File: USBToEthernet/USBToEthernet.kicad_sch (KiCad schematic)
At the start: 54 parts, among them J1 0480372200, J2 L836-1J1T-43, SW1 SW_Push, U1 LAN7500-ABJZ, U2 NCP1117-3.3_SOT223, U3 93LCxxAxxOT, U4 USBLC6-2SC6, U6 AMS1117-1.2, Y1 25Mhz

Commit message: Will redo layout
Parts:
- J1: footprint (none) -> USB_A_Plug:MOLEX_0480372200
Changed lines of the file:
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@@
 			)
 		)
-		(property "Footprint" ""
+		(property "Footprint" "USB_A_Plug:MOLEX_0480372200"
 			(at 19.812 16.256 0)
 			(effects

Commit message: Revamped the PCB
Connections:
- net TR0+: now also U1.43 (TR0P); no longer U1.44 (TR0P)
- net TR0-: now also U1.44 (TR0N); no longer U1.43 (TR0N)
- net TR2+: now also U1.51 (TR2P); no longer U1.52 (TR2P)
- net TR2-: now also U1.52 (TR2N); no longer U1.51 (TR2N)
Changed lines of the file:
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@@
 		)
 	)
-	(label "TR0-"
+	(label "TR0+"
 		(at 135.89 85.09 180)
 		(effects
@@
 		)
 	)
-	(label "TR2-"
+	(label "TR2+"
 		(at 135.89 100.33 180)
 		(effects
@@
 		)
 	)
-	(label "TR2+"
+	(label "TR2-"
 		(at 135.89 102.87 180)
 		(effects
@@
 		)
 	)
-	(label "TR0+"
+	(label "TR0-"
 		(at 135.89 87.63 180)
 		(effects
@@
 	)
 	(symbol
+		(lib_name "LAN7500-ABJZ_1")
 		(lib_id "Interface_Ethernet:LAN7500-ABJZ")
 		(at 53.34 101.6 0)
@@
 		(fields_autoplaced yes)
 		(property "Reference" "U1"
-			(at 55.4833 132.08 0)
+			(at 53.34 81.28 0)
 			(effects
 				(font
 					(size 1.27 1.27)
 				)
-				(justify left)
 			)
 		)
 		(property "Value" "LAN7500-ABJZ"
-			(at 55.4833 134.62 0)
+			(at 53.34 83.82 0)
 			(effects
 				(font
 					(size 1.27 1.27)
 				)
-				(justify left)
 			)
 		)

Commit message: Reroute again
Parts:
- C1, C10, C11, C12, C13, C14, C15, C16, C17, C18, C19, C2, C20, C21, C22, C23, C24, C25, C26, C27, C3, C4, C5, C6, C7, C8, C9: footprint Capacitor_SMD:C_0603_1608Metric -> Capacitor_SMD:C_0402_1005Metric
- FB1, FB2, FB3, FB4, FB5: footprint Inductor_SMD:L_0603_1608Metric -> Inductor_SMD:L_0402_1005Metric
- R1, R10, R11, R12, R13, R2, R3, R4, R5, R6, R7, R8, R9: footprint Resistor_SMD:R_0603_1608Metric -> Resistor_SMD:R_0402_1005Metric
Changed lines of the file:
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@@
 			)
 		)
-		(property "Footprint" "Capacitor_SMD:C_0603_1608Metric"
+		(property "Footprint" "Capacitor_SMD:C_0402_1005Metric"
 			(at 24.13 154.94 0)
 			(effects
@@
 			)
 		)
-		(property "Footprint" "Capacitor_SMD:C_0603_1608Metric"
+		(property "Footprint" "Capacitor_SMD:C_0402_1005Metric"
 			(at 129.54 160.02 0)
 			(effects
@@
 			)
 		)
-		(property "Footprint" "Inductor_SMD:L_0603_1608Metric"
+		(property "Footprint" "Inductor_SMD:L_0402_1005Metric"
 			(at 216.662 20.32 90)
 			(effects
@@
 			)
 		)
-		(property "Footprint" "Resistor_SMD:R_0603_1608Metric"
+		(property "Footprint" "Resistor_SMD:R_0402_1005Metric"
 			(at 99.06 109.22 0)
 			(effects
@@
 			)
 		)
-		(property "Footprint" "Capacitor_SMD:C_0603_1608Metric"
+		(property "Footprint" "Capacitor_SMD:C_0402_1005Metric"
 			(at 177.8 31.75 0)
 			(effects
@@
 			)
 		)
-		(property "Footprint" "Capacitor_SMD:C_0603_1608Metric"
+		(property "Footprint" "Capacitor_SMD:C_0402_1005Metric"
 			(at 30.48 154.94 0)
 			(effects
@@
 			)
 		)
-		(property "Footprint" "Capacitor_SMD:C_0603_1608Metric"
+		(property "Footprint" "Capacitor_SMD:C_0402_1005Metric"
 			(at 190.5 76.2 0)
 			(effects
@@
 			)
 		)
-		(property "Footprint" "Capacitor_SMD:C_0603_1608Metric"
+		(property "Footprint" "Capacitor_SMD:C_0402_1005Metric"
 			(at 63.5 154.94 0)
 			(effects
@@
 			)
 		)
-		(property "Footprint" "Resistor_SMD:R_0603_1608Metric"
+		(property "Footprint" "Resistor_SMD:R_0402_1005Metric"
 			(at 196.85 30.48 0)
 			(effects
@@
 			)
 		)
-		(property "Footprint" "Capacitor_SMD:C_0603_1608Metric"
+		(property "Footprint" "Capacitor_SMD:C_0402_1005Metric"
 			(at 90.17 35.56 0)
 			(effects
@@
 			)
 		)
-		(property "Footprint" "Capacitor_SMD:C_0603_1608Metric"
+		(property "Footprint" "Capacitor_SMD:C_0402_1005Metric"
 			(at 182.88 76.2 0)
 			(effects
@@
 			)
 		)
-		(property "Footprint" "Capacitor_SMD:C_0603_1608Metric"
+		(property "Footprint" "Capacitor_SMD:C_0402_1005Metric"
 			(at 17.78 154.94 0)
 			(effects
@@
 			)
 		)
-		(property "Footprint" "Capacitor_SMD:C_0603_1608Metric"
+		(property "Footprint" "Capacitor_SMD:C_0402_1005Metric"
 			(at 173.99 76.2 0)
 			(effects
@@
 			)
 		)
-		(property "Footprint" "Capacitor_SMD:C_0603_1608Metric"
+		(property "Footprint" "Capacitor_SMD:C_0402_1005Metric"
 			(at 121.92 185.42 0)
 			(effects
@@
 			)
 		)
-		(property "Footprint" "Capacitor_SMD:C_0603_1608Metric"
+		(property "Footprint" "Capacitor_SMD:C_0402_1005Metric"
 			(at 128.27 31.75 0)
 			(effects
@@
 			)
 		)
-		(property "Footprint" "Capacitor_SMD:C_0603_1608Metric"
+		(property "Footprint" "Capacitor_SMD:C_0402_1005Metric"
 			(at 69.85 184.15 0)
 			(effects
@@
 			)
 		)
-		(property "Footprint" "Capacitor_SMD:C_0603_1608Metric"
+		(property "Footprint" "Capacitor_SMD:C_0402_1005Metric"
 			(at 87.63 160.02 0)
 			(effects
@@
 			)
 		)
-		(property "Footprint" "Inductor_SMD:L_0603_1608Metric"
+		(property "Footprint" "Inductor_SMD:L_0402_1005Metric"
 			(at 82.042 149.86 90)
 			(effects
@@
 			)
 		)
-		(property "Footprint" "Capacitor_SMD:C_0603_1608Metric"
+		(property "Footprint" "Capacitor_SMD:C_0402_1005Metric"
 			(at 153.67 76.2 0)
 			(effects
@@
 			)
 		)
-		(property "Footprint" "Capacitor_SMD:C_0603_1608Metric"
+		(property "Footprint" "Capacitor_SMD:C_0402_1005Metric"
 			(at 210.82 31.75 0)
 			(effects
@@
 			)
 		)
-		(property "Footprint" "Capacitor_SMD:C_0603_1608Metric"
+		(property "Footprint" "Capacitor_SMD:C_0402_1005Metric"
 			(at 107.95 160.02 0)
 			(effects
@@
 			)
 		)
-		(property "Footprint" "Resistor_SMD:R_0603_1608Metric"
+		(property "Footprint" "Resistor_SMD:R_0402_1005Metric"
 			(at 264.16 30.48 0)
 			(effects
@@
 			)
 		)
-		(property "Footprint" "Capacitor_SMD:C_0603_1608Metric"
+		(property "Footprint" "Capacitor_SMD:C_0402_1005Metric"
 			(at 242.57 31.75 0)
 			(effects
@@
 			)
 		)
-		(property "Footprint" "Resistor_SMD:R_0603_1608Metric"
+		(property "Footprint" "Resistor_SMD:R_0402_1005Metric"
 			(at 200.66 30.48 0)
 			(effects
@@
 			)
 		)
-		(property "Footprint" "Capacitor_SMD:C_0603_1608Metric"
+		(property "Footprint" "Capacitor_SMD:C_0402_1005Metric"
 			(at 66.04 24.13 0)
 			(effects
@@
 			)
 		)
-		(property "Footprint" "Resistor_SMD:R_0603_1608Metric"
+		(property "Footprint" "Resistor_SMD:R_0402_1005Metric"
 			(at 260.35 30.48 0)
 			(effects
@@
 			)
 		)
-		(property "Footprint" "Capacitor_SMD:C_0603_1608Metric"
+		(property "Footprint" "Capacitor_SMD:C_0402_1005Metric"
 			(at 274.32 31.75 0)
 			(effects
@@
 			)
 		)
-		(property "Footprint" "Capacitor_SMD:C_0603_1608Metric"
+		(property "Footprint" "Capacitor_SMD:C_0402_1005Metric"
 			(at 107.95 34.29 0)
 			(effects
@@
 			)
 		)
-		(property "Footprint" "Resistor_SMD:R_0603_1608Metric"
+		(property "Footprint" "Resistor_SMD:R_0402_1005Metric"
 			(at 163.83 30.48 0)
 			(effects
@@
 			)
 		)
-		(property "Footprint" "Capacitor_SMD:C_0603_1608Metric"
+		(property "Footprint" "Capacitor_SMD:C_0402_1005Metric"
 			(at 36.83 154.94 0)
 			(effects
@@
 			)
 		)
-		(property "Footprint" "Capacitor_SMD:C_0603_1608Metric"
+		(property "Footprint" "Capacitor_SMD:C_0402_1005Metric"
 			(at 146.05 31.75 0)
 			(effects
@@
 			)
 		)
-		(property "Footprint" "Resistor_SMD:R_0603_1608Metric"
+		(property "Footprint" "Resistor_SMD:R_0402_1005Metric"
 			(at 241.3 93.98 0)
 			(effects
@@
 			)
 		)
-		(property "Footprint" "Resistor_SMD:R_0603_1608Metric"
+		(property "Footprint" "Resistor_SMD:R_0402_1005Metric"
 			(at 242.57 86.36 0)
 			(effects
@@
 			)
 		)
-		(property "Footprint" "Capacitor_SMD:C_0603_1608Metric"
+		(property "Footprint" "Capacitor_SMD:C_0402_1005Metric"
 			(at 43.18 154.94 0)
 			(effects
@@
 			)
 		)
-		(property "Footprint" "Capacitor_SMD:C_0603_1608Metric"
+		(property "Footprint" "Capacitor_SMD:C_0402_1005Metric"
 			(at 87.63 184.15 0)
 			(effects
@@
 			)
 		)
-		(property "Footprint" "Resistor_SMD:R_0603_1608Metric"
+		(property "Footprint" "Resistor_SMD:R_0402_1005Metric"
 			(at 91.44 106.68 0)
 			(effects
@@
 			)
 		)
-		(property "Footprint" "Capacitor_SMD:C_0603_1608Metric"
+		(property "Footprint" "Capacitor_SMD:C_0402_1005Metric"
 			(at 49.53 154.94 0)
 			(effects
@@
 			)
 		)
-		(property "Footprint" "Inductor_SMD:L_0603_1608Metric"
+		(property "Footprint" "Inductor_SMD:L_0402_1005Metric"
 			(at 102.362 149.86 90)
 			(effects
@@
 			)
 		)
-		(property "Footprint" "Capacitor_SMD:C_0603_1608Metric"
+		(property "Footprint" "Capacitor_SMD:C_0402_1005Metric"
 			(at 198.12 76.2 0)
 			(effects
@@
 			)
 		)
-		(property "Footprint" "Inductor_SMD:L_0603_1608Metric"
+		(property "Footprint" "Inductor_SMD:L_0402_1005Metric"
 			(at 148.082 67.31 90)
 			(effects
@@
 			)
 		)
-		(property "Footprint" "Resistor_SMD:R_0603_1608Metric"
+		(property "Footprint" "Resistor_SMD:R_0402_1005Metric"
 			(at 228.6 30.48 0)
 			(effects
@@
 			)
 		)
-		(property "Footprint" "Resistor_SMD:R_0603_1608Metric"
+		(property "Footprint" "Resistor_SMD:R_0402_1005Metric"
 			(at 167.64 30.48 0)
 			(effects
@@
 			)
 		)
-		(property "Footprint" "Resistor_SMD:R_0603_1608Metric"
+		(property "Footprint" "Resistor_SMD:R_0402_1005Metric"
 			(at 121.92 175.26 0)
 			(effects
@@
 			)
 		)
-		(property "Footprint" "Resistor_SMD:R_0603_1608Metric"
+		(property "Footprint" "Resistor_SMD:R_0402_1005Metric"
 			(at 232.41 30.48 0)
 			(effects
@@
 			)
 		)
-		(property "Footprint" "Inductor_SMD:L_0603_1608Metric"
+		(property "Footprint" "Inductor_SMD:L_0402_1005Metric"
 			(at 123.952 151.13 90)
 			(effects

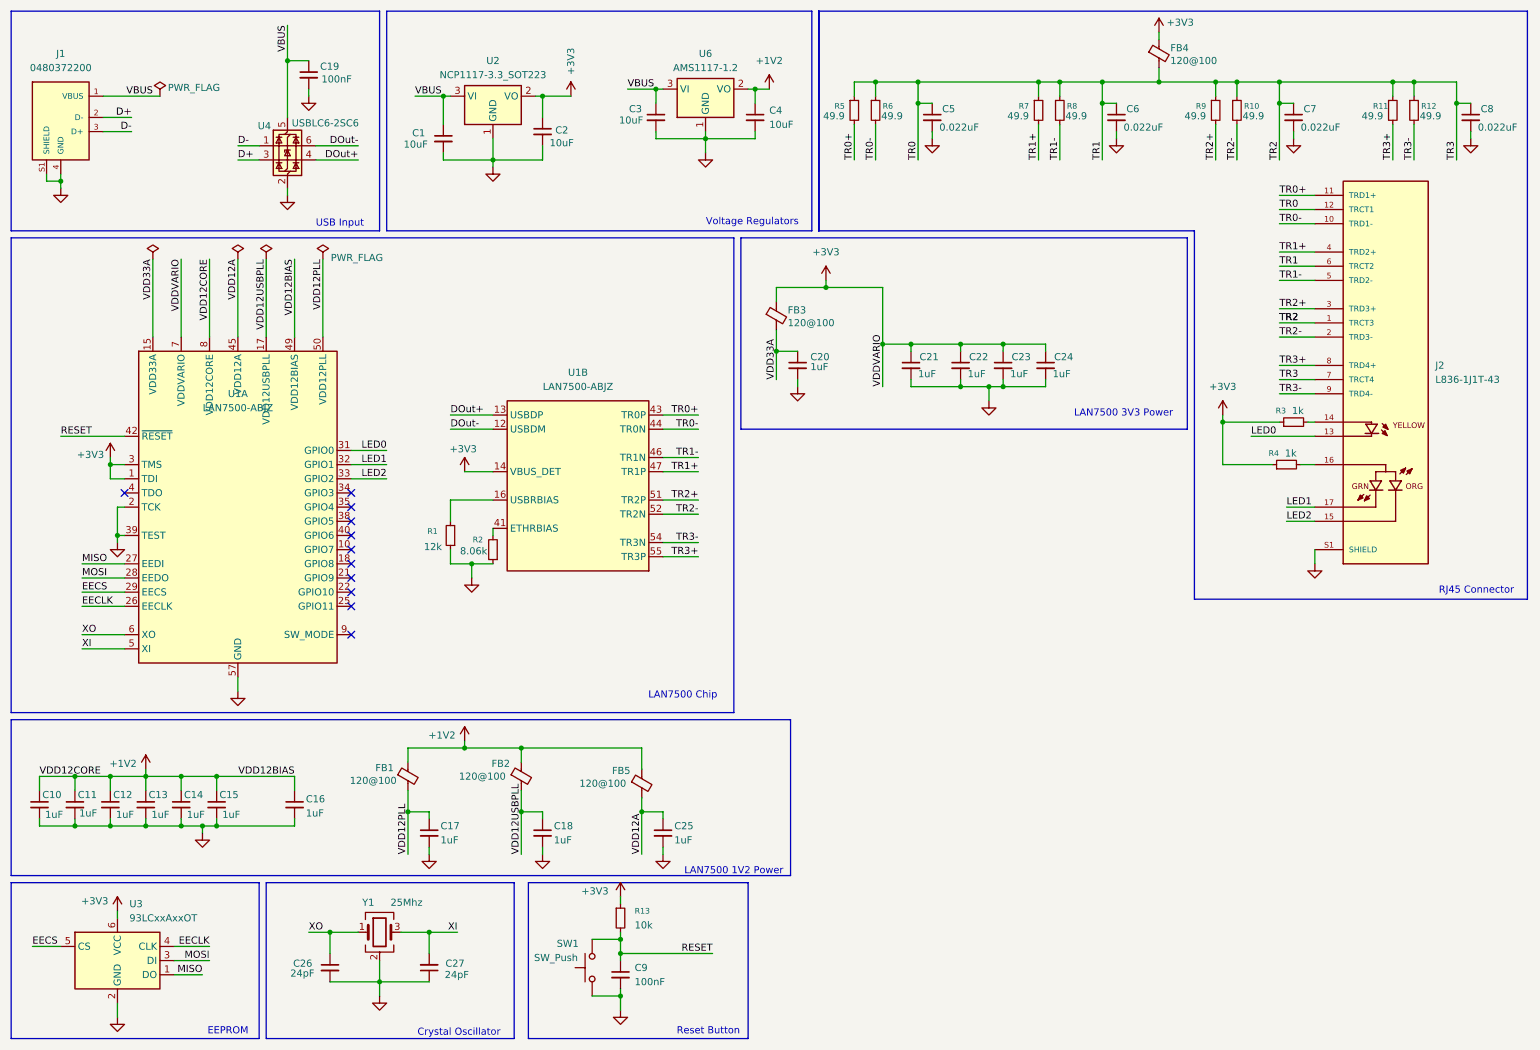
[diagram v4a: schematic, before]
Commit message: Added more space between capacitors
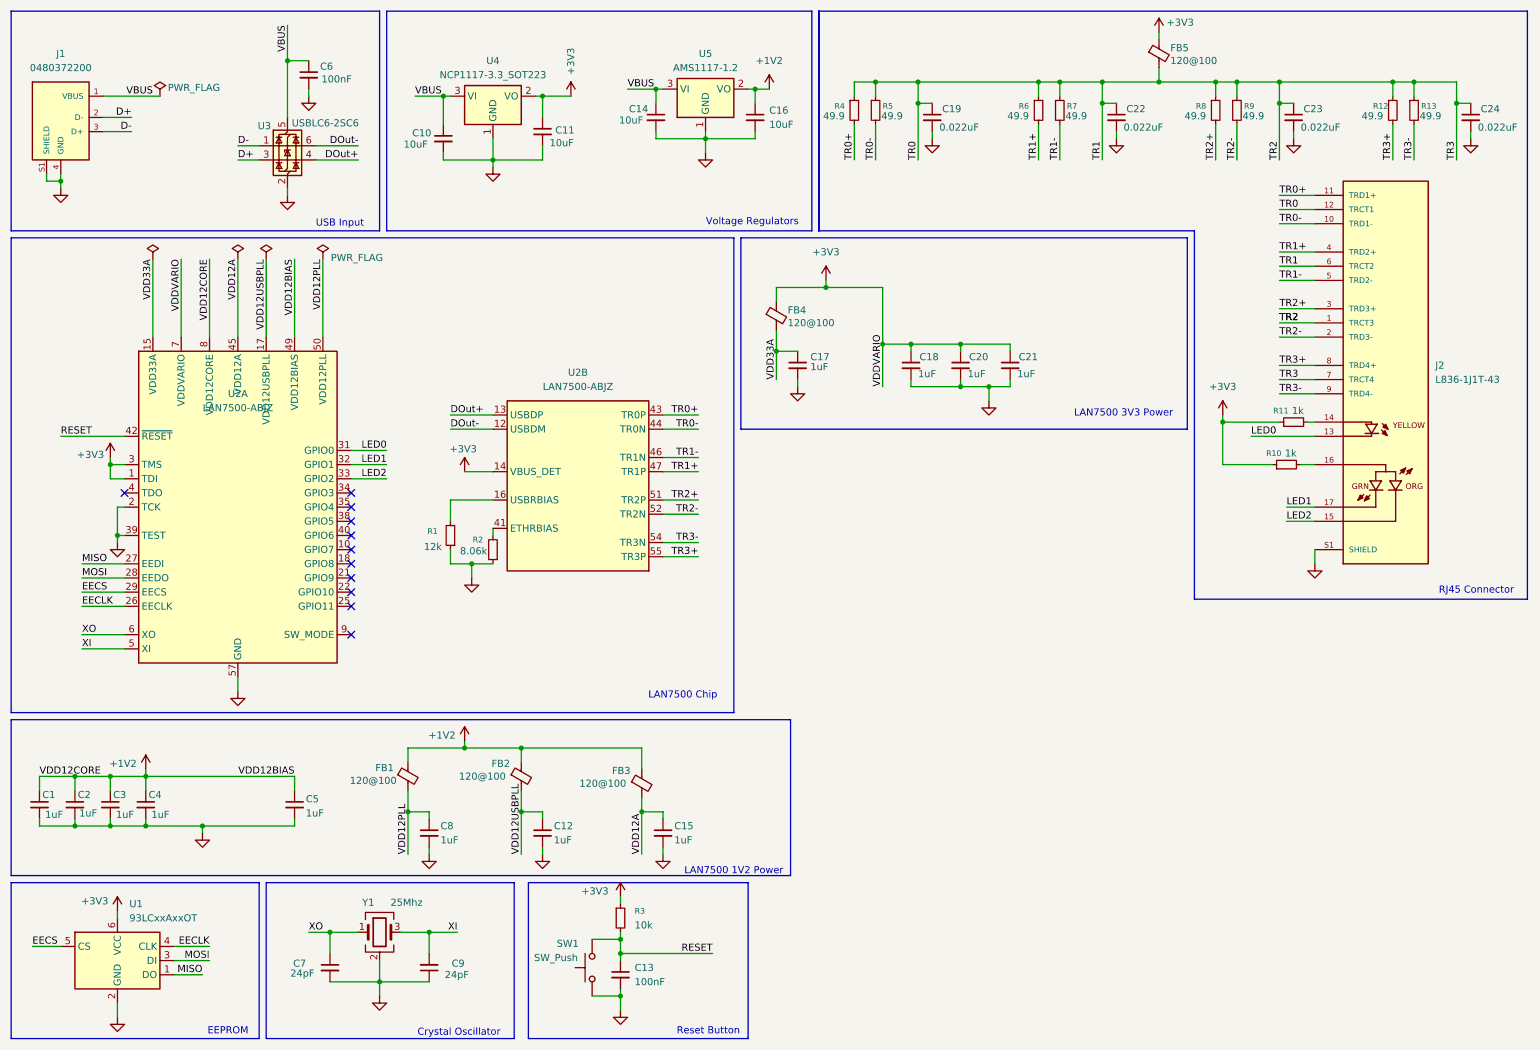
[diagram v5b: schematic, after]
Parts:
- removed C13, C15, C23: 1uF, Capacitor_SMD:C_0402_1005Metric, symbol Device:C_Small
- C5: renamed from C16; footprint Capacitor_SMD:C_0402_1005Metric -> Capacitor_SMD:C_0402_1005Metric_Pad0.74x0.62mm_HandSolder
- C8: renamed from C17; footprint Capacitor_SMD:C_0402_1005Metric -> Capacitor_SMD:C_0402_1005Metric_Pad0.74x0.62mm_HandSolder
- FB1, FB2: footprint Inductor_SMD:L_0402_1005Metric -> Inductor_SMD:L_0402_1005Metric_Pad0.77x0.64mm_HandSolder
- R1: footprint Resistor_SMD:R_0402_1005Metric -> Resistor_SMD:R_0402_1005Metric_Pad0.72x0.64mm_HandSolder
- renumbered C10 to C1, C1 to C10, C2 to C11, C18 to C12, C9 to C13, C3 to C14, C25 to C15, C4 to C16, C20 to C17, C21 to C18, C5 to C19, C11 to C2, C22 to C20, C24 to C21, C6 to C22, C7 to C23, C8 to C24, C12 to C3, C14 to C4, C19 to C6, C26 to C7, C27 to C9, FB5 to FB3, FB3 to FB4, FB4 to FB5, R4 to R10, R3 to R11, R11 to R12, R12 to R13, R13 to R3, R5 to R4, R6 to R5, R7 to R6, R8 to R7, R9 to R8, R10 to R9, U3 to U1, U1 to U2, U4 to U3, U2 to U4, U6 to U5
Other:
- moved on the sheet: C21, C4
